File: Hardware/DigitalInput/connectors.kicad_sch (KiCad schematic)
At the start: 12 parts, among them J1 DIGITAL INPUT, J2 DIGITAL OUTPUT, J3 Conn_02x23_Odd_Even, J4 Conn_02x23_Odd_Even

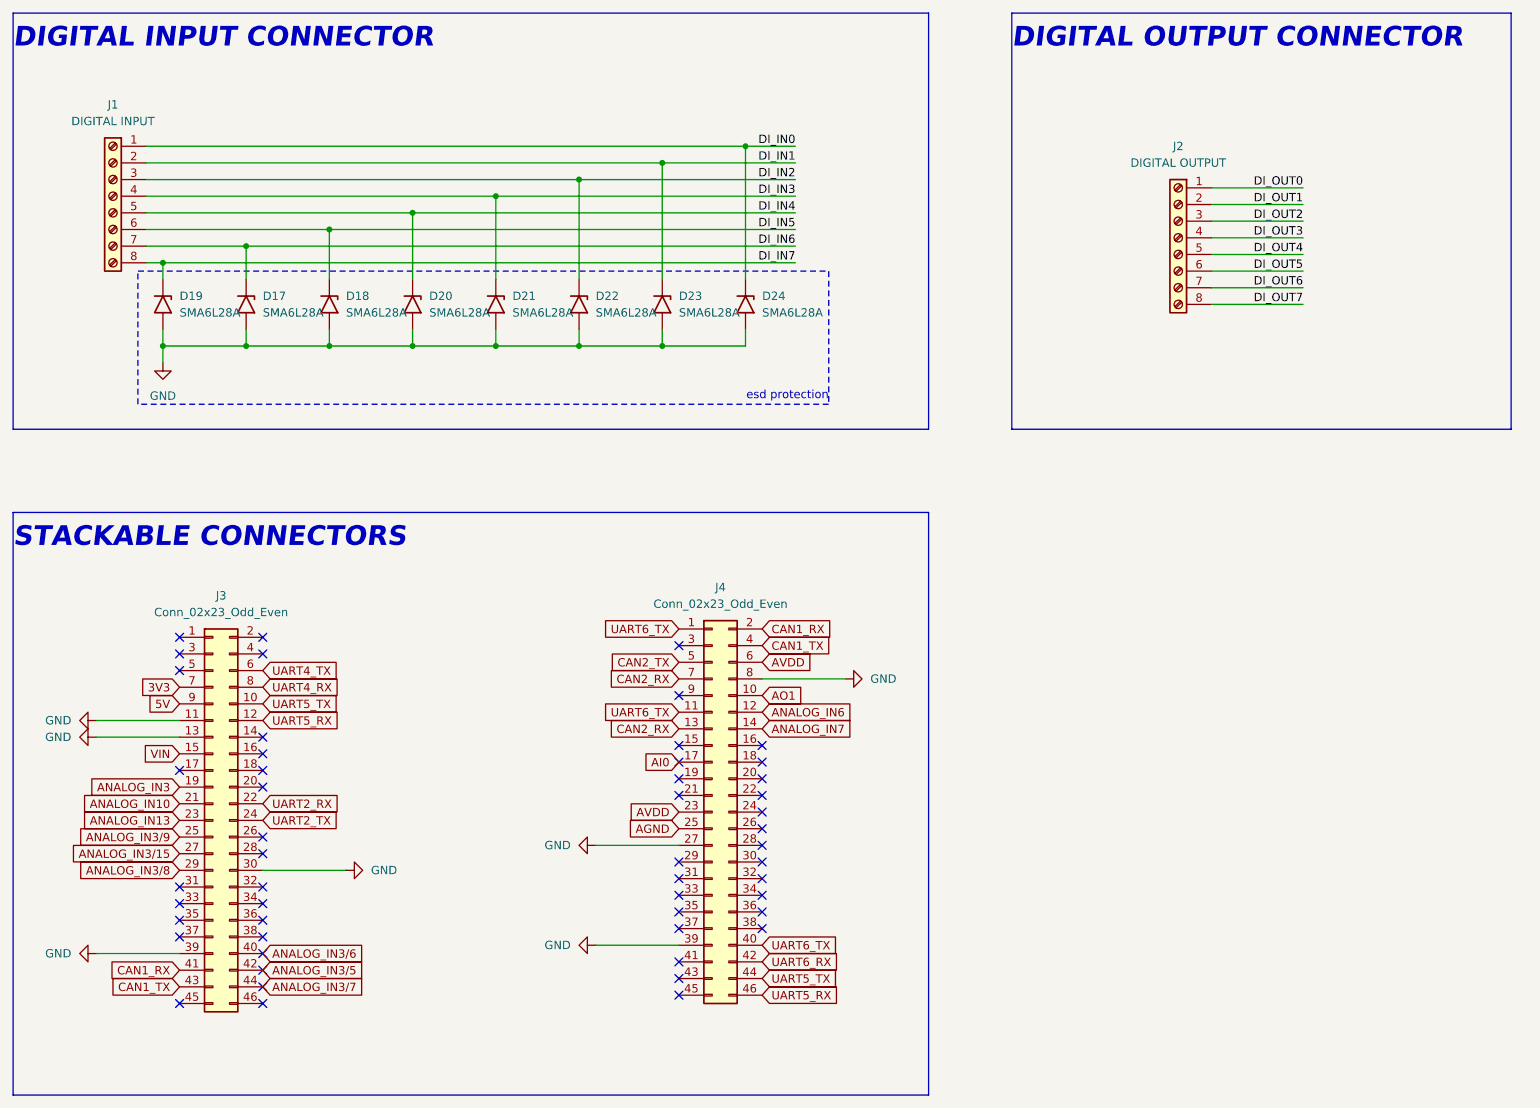
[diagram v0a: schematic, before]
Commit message: digital output & digital input update
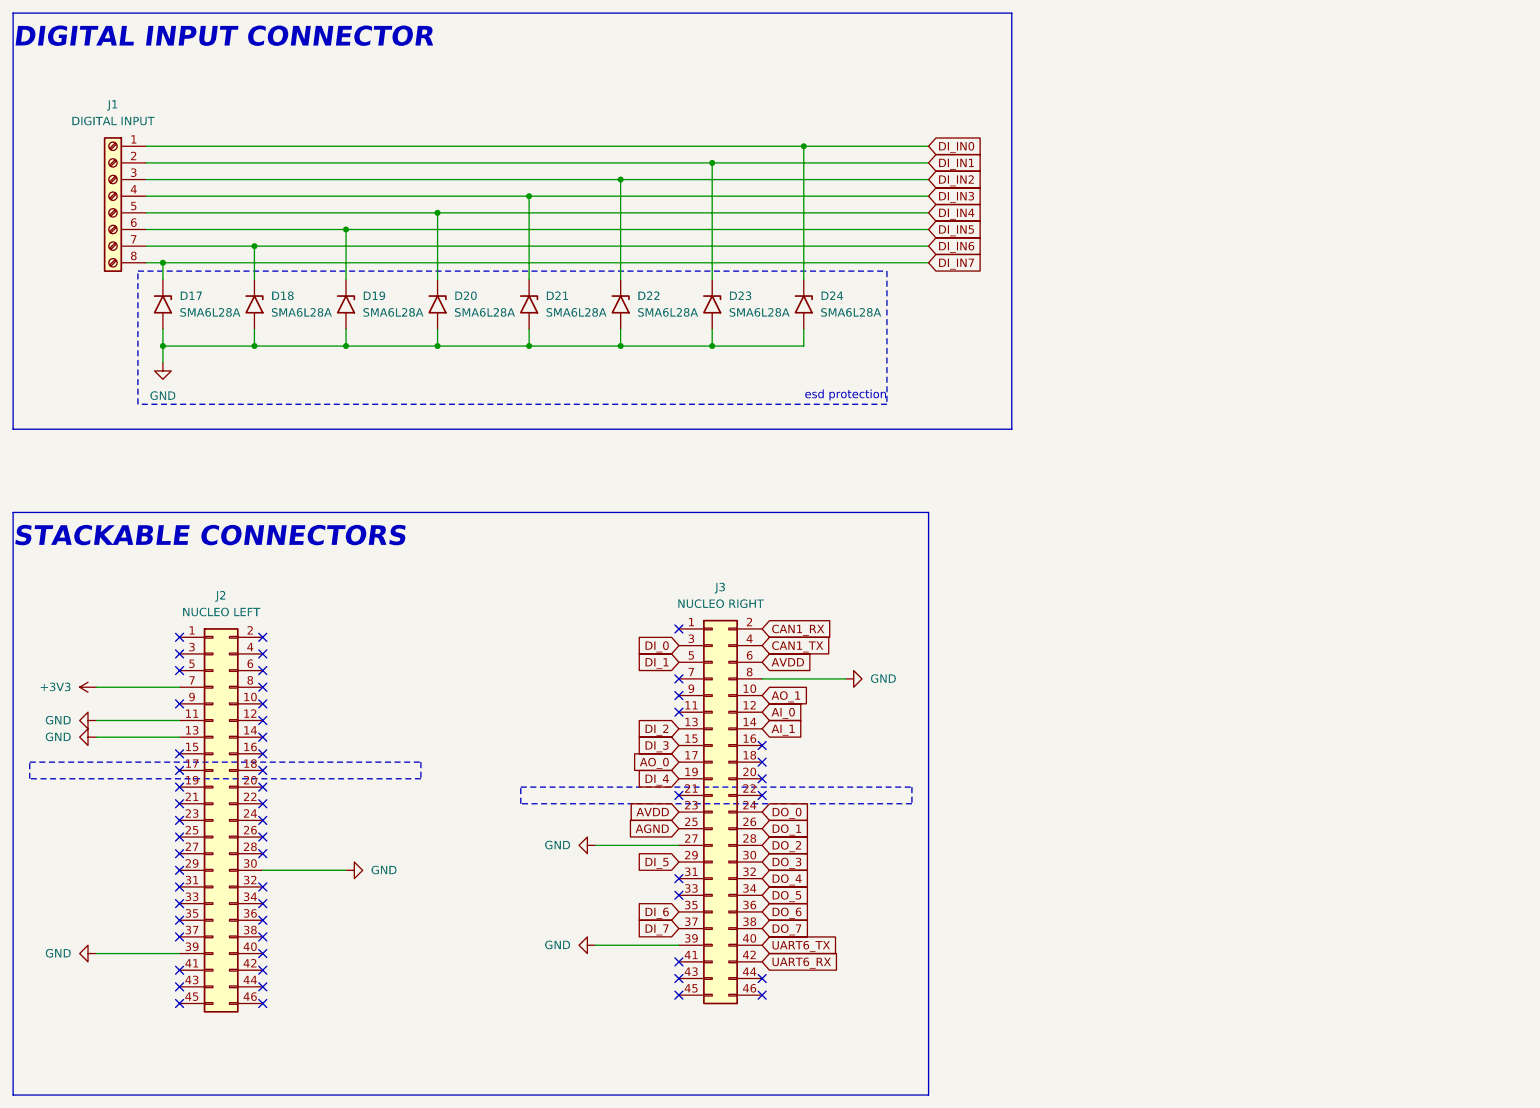
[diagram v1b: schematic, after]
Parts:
- removed J2: DIGITAL OUTPUT, PLC_STM:1725711, symbol Connector:Screw_Terminal_01x08
- removed J4: Conn_02x23_Odd_Even, PLC_STM:PRT12790, symbol Connector_Generic:Conn_02x23_Odd_Even
- added J2: NUCLEO LEFT, PLC_STM:PRT12790, symbol Connector_Generic:Conn_02x23_Odd_Even
- J3: value Conn_02x23_Odd_Even -> NUCLEO RIGHT
- renumbered D19 to D17, D17 to D18, D18 to D19
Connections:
- net ANALOG_IN13 is gone; now on net AVDD: J3.23 (Pin_23)
- net ANALOG_IN3/15 is gone; now on net GND: J3.27 (Pin_27)
- net ANALOG_IN3/5 is gone; now on net UART6_RX: J3.42 (Pin_42)
- net ANALOG_IN3/6 is gone; now on net UART6_TX: J3.40 (Pin_40)
- net ANALOG_IN3/9 is gone; now on net AGND: J3.25 (Pin_25)
- net UART4_RX is gone; now on net GND: J3.8 (Pin_8)
- net UART4_TX is gone; now on net AVDD: J3.6 (Pin_6)
- net CAN1_RX: now also J3.2 (Pin_2); no longer J3.41 (Pin_41)
- net CAN1_TX: now also J3.4 (Pin_4); no longer J3.43 (Pin_43)
- net GND: now also J2.11 (Pin_11), J2.13 (Pin_13), J2.30 (Pin_30), J2.39 (Pin_39); no longer J3.11 (Pin_11), J3.13 (Pin_13), J3.30 (Pin_30)
- net AI_1: now reaches J3.14 (Pin_14)
- net AO_0: now reaches J3.17 (Pin_17)
- net DO_1: now reaches J3.26 (Pin_26)
- net DO_2: now reaches J3.28 (Pin_28)
- net DI_0: now reaches J3.3 (Pin_3)
- net DO_4: now reaches J3.32 (Pin_32)
- net DO_5: now reaches J3.34 (Pin_34)
- net DI_6: now reaches J3.35 (Pin_35)
- net DO_6: now reaches J3.36 (Pin_36)
- net DI_7: now reaches J3.37 (Pin_37)
- net DO_7: now reaches J3.38 (Pin_38)
- net DI_1: now reaches J3.5 (Pin_5)
- net 3V3: no longer names the net of J3.7 (Pin_7)
- net 5V: no longer names the net of J3.9 (Pin_9)
- net ANALOG_IN10: no longer names the net of J3.21 (Pin_21)
- net ANALOG_IN3 renamed DI_4
- net ANALOG_IN3/7: no longer names the net of J3.44 (Pin_44)
- net ANALOG_IN3/8 renamed DI_5
- net UART2_RX: no longer names the net of J3.22 (Pin_22)
- net UART2_TX renamed DO_0
- net UART5_RX renamed AI_0
- net UART5_TX renamed AO_1
- net VIN renamed DI_3
- new net +3V3: J2.7 (Pin_7)
- new net DI_2: J3.13 (Pin_13)
- new net DO_3: J3.30 (Pin_30)
- no-connect marks 51 -> 57
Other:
- note removed: "DIGITAL OUTPUT CONNECTOR"
- moved on the sheet: D18, D19, D20, D21, D22, D23, D24

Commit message: digital input finished
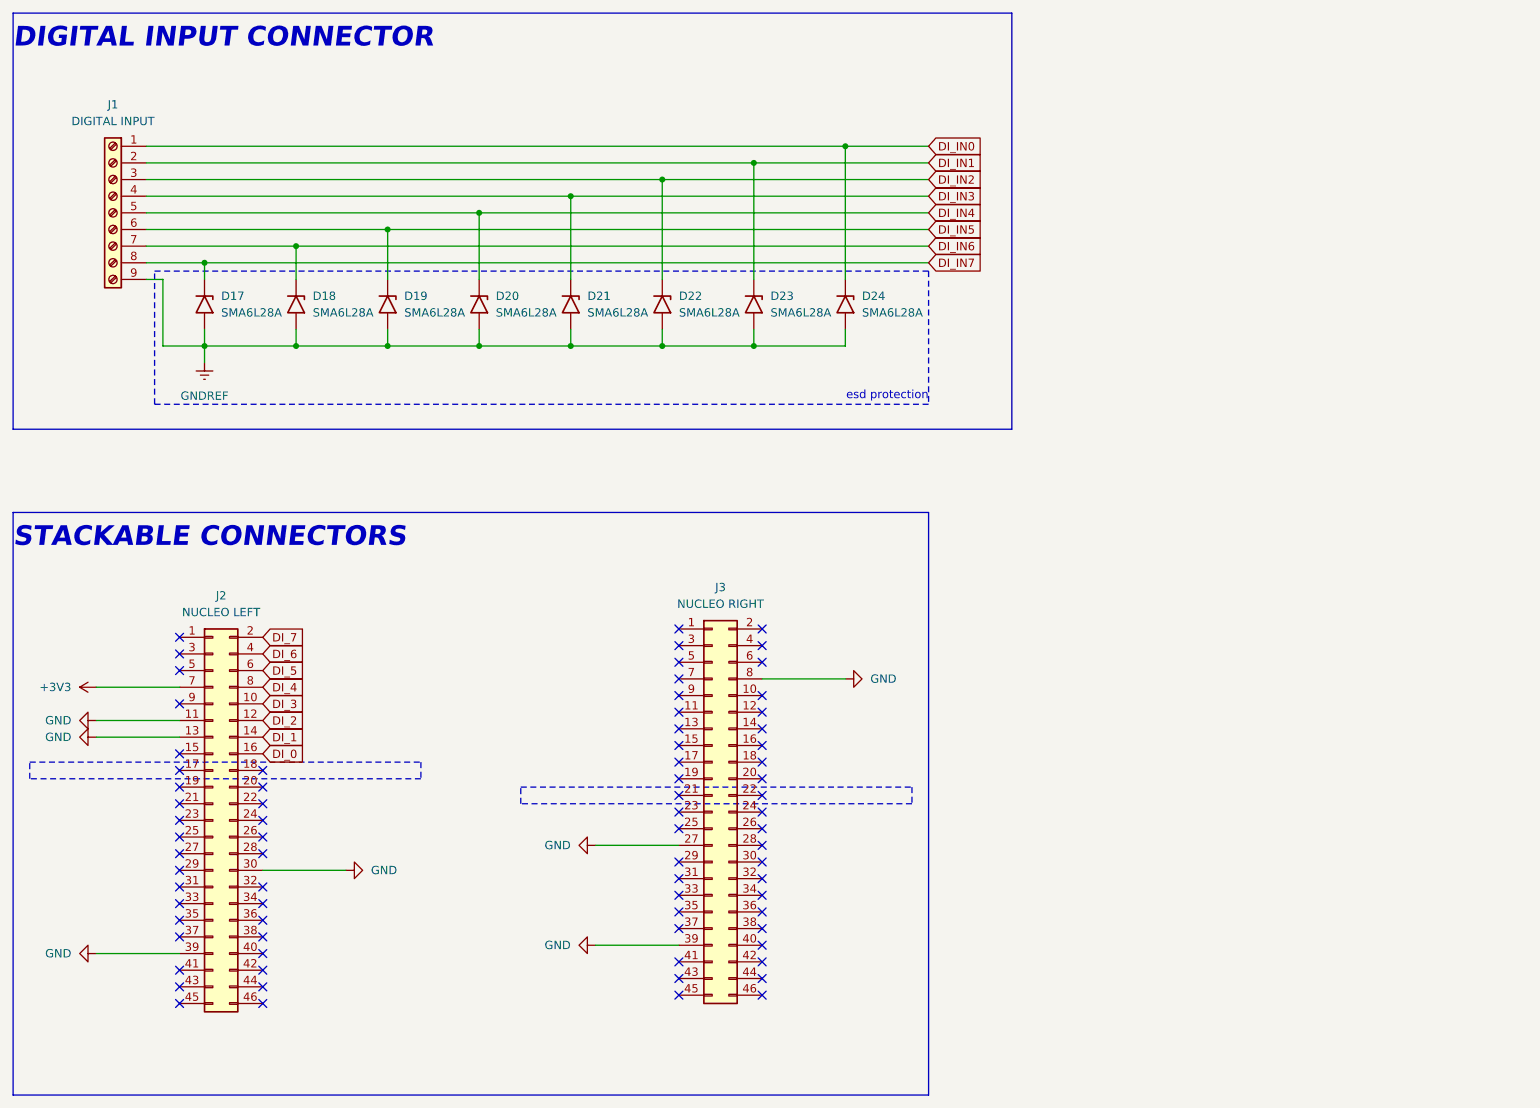
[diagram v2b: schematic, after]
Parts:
- removed J1: DIGITAL INPUT, PLC_STM:1725711, symbol Connector:Screw_Terminal_01x08
- added J1: DIGITAL INPUT, PLC_STM:1725724, symbol Connector:Screw_Terminal_01x09
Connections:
- net DI_0: now also J2.16 (Pin_16); no longer J3.3 (Pin_3)
- net DI_1: now also J2.14 (Pin_14); no longer J3.5 (Pin_5)
- net DI_2: now also J2.12 (Pin_12); no longer J3.13 (Pin_13)
- net DI_3: now also J2.10 (Pin_10); no longer J3.15 (Pin_15)
- net DI_4: now also J2.8 (Pin_8); no longer J3.19 (Pin_19)
- net DI_5: now also J2.6 (Pin_6); no longer J3.29 (Pin_29)
- net DI_6: now also J2.4 (Pin_4); no longer J3.35 (Pin_35)
- net DI_7: now also J2.2 (Pin_2); no longer J3.37 (Pin_37)
- net DI_IN0: now also J1.1 (Pin_1)
- net DI_IN1: now also J1.2 (Pin_2)
- net DI_IN2: now also J1.3 (Pin_3)
- net DI_IN3: now also J1.4 (Pin_4)
- net DI_IN4: now also J1.5 (Pin_5)
- net DI_IN5: now also J1.6 (Pin_6)
- net DI_IN6: now also J1.7 (Pin_7)
- net DI_IN7: now also J1.8 (Pin_8)
- net GND: no longer D17.2 (A2), D18.2 (A2), D19.2 (A2), D20.2 (A2), D21.2 (A2), D22.2 (A2), D23.2 (A2), D24.2 (A2)
- net AGND: no longer names the net of J3.25 (Pin_25)
- net AI_0: no longer names the net of J3.12 (Pin_12)
- net AI_1: no longer names the net of J3.14 (Pin_14)
- net AO_0: no longer names the net of J3.17 (Pin_17)
- net AO_1: no longer names the net of J3.10 (Pin_10)
- net AVDD: no longer names the net of J3.23 (Pin_23)
- net AVDD: no longer J3.6 (Pin_6)
- net CAN1_RX: no longer names the net of J3.2 (Pin_2)
- net CAN1_TX: no longer names the net of J3.4 (Pin_4)
- net DO_0: no longer names the net of J3.24 (Pin_24)
- net DO_1: no longer names the net of J3.26 (Pin_26)
- net DO_2: no longer names the net of J3.28 (Pin_28)
- net DO_3: no longer names the net of J3.30 (Pin_30)
- net DO_4: no longer names the net of J3.32 (Pin_32)
- net DO_5: no longer names the net of J3.34 (Pin_34)
- net DO_6: no longer names the net of J3.36 (Pin_36)
- net DO_7: no longer names the net of J3.38 (Pin_38)
- net UART6_RX: no longer names the net of J3.42 (Pin_42)
- net UART6_TX: no longer names the net of J3.40 (Pin_40)
- new net GNDREF: D17.2 (A2), D18.2 (A2), D19.2 (A2), D20.2 (A2), D21.2 (A2), D22.2 (A2), D23.2 (A2), D24.2 (A2), J1.9 (Pin_9)
- no-connect marks 57 -> 76
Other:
- moved on the sheet: D17, D18, D19, D20, D21, D22, D23, D24

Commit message: digital input pins update
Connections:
- net DI_0: now also J2.29 (Pin_29); no longer J2.16 (Pin_16)
- net DI_1: now also J2.23 (Pin_23); no longer J2.14 (Pin_14)
- net DI_2: now also J2.21 (Pin_21); no longer J2.12 (Pin_12)
- net DI_3: now also J2.19 (Pin_19); no longer J2.10 (Pin_10)
- net DI_4: now also J2.14 (Pin_14); no longer J2.8 (Pin_8)
- net DI_5: now also J2.8 (Pin_8); no longer J2.6 (Pin_6)
- net DI_6: now also J2.2 (Pin_2); no longer J2.4 (Pin_4)
- net DI_7: now also J3.18 (Pin_18); no longer J2.2 (Pin_2)

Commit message: digital input update
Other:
- note added: "DO LEFT: PC1, PC0, PD3, PG2, PG3, PE2, PE4, PE5 RIGHT: PC4, PF5, PF4, PE8, PF10, PE7, PD14, PF14 DI LEFT: PC2, PC3, PC0, PC1 RIGHT: PC8, PC6, PC5, PB2"
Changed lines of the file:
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@@
+		)
+	)
+	(text "DO\nLEFT:\nPC1, PC0, PD3, PG2, PG3, PE2, PE4, PE5\nRIGHT:\nPC4, PF5, PF4, PE8, PF10, PE7, PD14, PF14\n\nDI\nLEFT:\nPC2, PC3, PC0, PC1\n\nRIGHT:\nPC8, PC6, PC5, PB2 "
+		(exclude_from_sim no)
+		(at 170.18 115.824 0)
+		(effects
+			(font
+				(size 1.27 1.27)
+			)
+			(justify left)
 		)
 	)

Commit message: digital output & power finished
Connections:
- net +3V3: now also J2.25 (Pin_25); no longer J2.7 (Pin_7)
- net DI_0: now also J2.36 (Pin_36); no longer J2.29 (Pin_29)
- net DI_1: now also J2.35 (Pin_35); no longer J2.23 (Pin_23)
- net DI_2: now also J2.38 (Pin_38); no longer J2.21 (Pin_21)
- net DI_3: now also J2.37 (Pin_37); no longer J2.19 (Pin_19)
- net DI_4: now also J3.2 (Pin_2); no longer J2.14 (Pin_14)
- net DI_5: now also J3.4 (Pin_4); no longer J2.8 (Pin_8)
- net DI_6: now also J3.6 (Pin_6); no longer J2.2 (Pin_2)
- net DI_7: now also J3.22 (Pin_22); no longer J3.18 (Pin_18)
- net GND: now also J2.19 (Pin_19), J2.20 (Pin_20), J2.22 (Pin_22), J2.8 (Pin_8), J3.20 (Pin_20), J3.9 (Pin_9); no longer J2.11 (Pin_11), J2.13 (Pin_13), J2.30 (Pin_30), J2.39 (Pin_39), J3.27 (Pin_27), J3.39 (Pin_39), J3.8 (Pin_8)
- no-connect marks 76 -> 77
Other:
- moved on the sheet: J2
